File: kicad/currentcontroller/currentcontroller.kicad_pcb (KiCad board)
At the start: 2 copper layers, 86.4 x 53.3 mm, 39 parts, among them J1 Conn_01x04, J3 Conn_01x02, J4 Conn_01x04, Q1 IRF540N, U1 LM358, U2 MCP4822, U3 PC817, U4 PC817, U5 ATmega328P-P, U6 LM317_TO-220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

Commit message: Missing 5V trace
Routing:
- net +5V: track 164.1 -> 190.7 mm, vias 1 -> 2
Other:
- board text added: "Current controller Isolated (5 kV max) 2022-Dez www.tspi.at"
- board text removed: "Current controller Isolated (5 kV max) 76b595f / 2022-Nov www.tspi.at"
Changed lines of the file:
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@@
   (gr_rect (start 157.48 76.2) (end 243.84 129.54) (layer "Edge.Cuts") (width 0.1) (fill none))
   (gr_rect (start 219.71 106.68) (end 222.885 123.19) (layer "Edge.Cuts") (width 0.1) (fill none))
-  (gr_text "Current controller\nIsolated (5 kV max)\n76b595f / 2022-Nov\nwww.tspi.at" (at 219.71 99.695) (layer "F.SilkS")
+  (gr_text "Current controller\nIsolated (5 kV max)\n2022-Dez\nwww.tspi.at" (at 219.71 99.695) (layer "F.SilkS")
     (effects (font (size 1 1) (thickness 0.15)) (justify left))
   )
@@
   )
   (segment (start 184.15 102.91) (end 185.42 104.18) (width 0.25) (layer "F.Cu") (net 1))
+  (segment (start 181.61 93.98) (end 184.15 96.52) (width 0.25) (layer "F.Cu") (net 1))
   (segment (start 218.948 111.257) (end 218.948 93.218) (width 0.6) (layer "F.Cu") (net 1))
   (segment (start 187.96 80.01) (end 189.738 78.232) (width 0.25) (layer "F.Cu") (net 1))
@@
   (segment (start 185.42 104.18) (end 185.42 114.3) (width 0.25) (layer "F.Cu") (net 1))
   (segment (start 165.7325 112.99) (end 166.615 113.8725) (width 0.6) (layer "F.Cu") (net 1))
+  (segment (start 184.15 96.52) (end 184.15 102.91) (width 0.25) (layer "F.Cu") (net 1))
   (segment (start 185.674 125.984) (end 186.182 126.492) (width 0.6) (layer "F.Cu") (net 1))
   (segment (start 213.36 86.36) (end 215.9 86.36) (width 0.25) (layer "F.Cu") (net 1))
@@
   (segment (start 189.738 78.232) (end 198.882 78.232) (width 0.25) (layer "F.Cu") (net 1))
   (segment (start 185.42 125.984) (end 185.674 125.984) (width 0.6) (layer "F.Cu") (net 1))
+  (via (at 181.61 93.98) (size 0.8) (drill 0.4) (layers "F.Cu" "B.Cu") (net 1))
   (via (at 191.008 104.14) (size 0.8) (drill 0.4) (layers "F.Cu" "B.Cu") (net 1))
   (segment (start 185.38 104.14) (end 191.008 104.14) (width 0.25) (layer "B.Cu") (net 1))
   (segment (start 184.15 102.91) (end 185.38 104.14) (width 0.25) (layer "B.Cu") (net 1))
+  (segment (start 187.96 80.01) (end 184.333601 83.636399) (width 0.25) (layer "B.Cu") (net 1))
+  (segment (start 181.61 90.17) (end 181.61 93.98) (width 0.25) (layer "B.Cu") (net 1))
+  (segment (start 184.333601 83.636399) (end 184.333601 87.446399) (width 0.25) (layer "B.Cu") (net 1))
   (segment (start 185.42 125.73) (end 186.182 126.492) (width 0.25) (layer "B.Cu") (net 1))
   (segment (start 185.42 114.3) (end 185.42 125.73) (width 0.25) (layer "B.Cu") (net 1))
+  (segment (start 184.333601 87.446399) (end 181.61 90.17) (width 0.25) (layer "B.Cu") (net 1))
   (segment (start 162.56 109.22) (end 162.56 107.99) (width 0.25) (layer "F.Cu") (net 2))
   (segment (start 167.315 109.6475) (end 167.315 110.815) (width 0.25) (layer "F.Cu") (net 2))
@@
     (connect_pads (clearance 0.508))
     (min_thickness 0.254) (filled_areas_thickness no)
-    (fill yes (thermal_gap 0.508) (thermal_bridge_width 0.508) (smoothing fillet))
+    (fill (thermal_gap 0.508) (thermal_bridge_width 0.508) (smoothing fillet))
     (polygon
       (pts

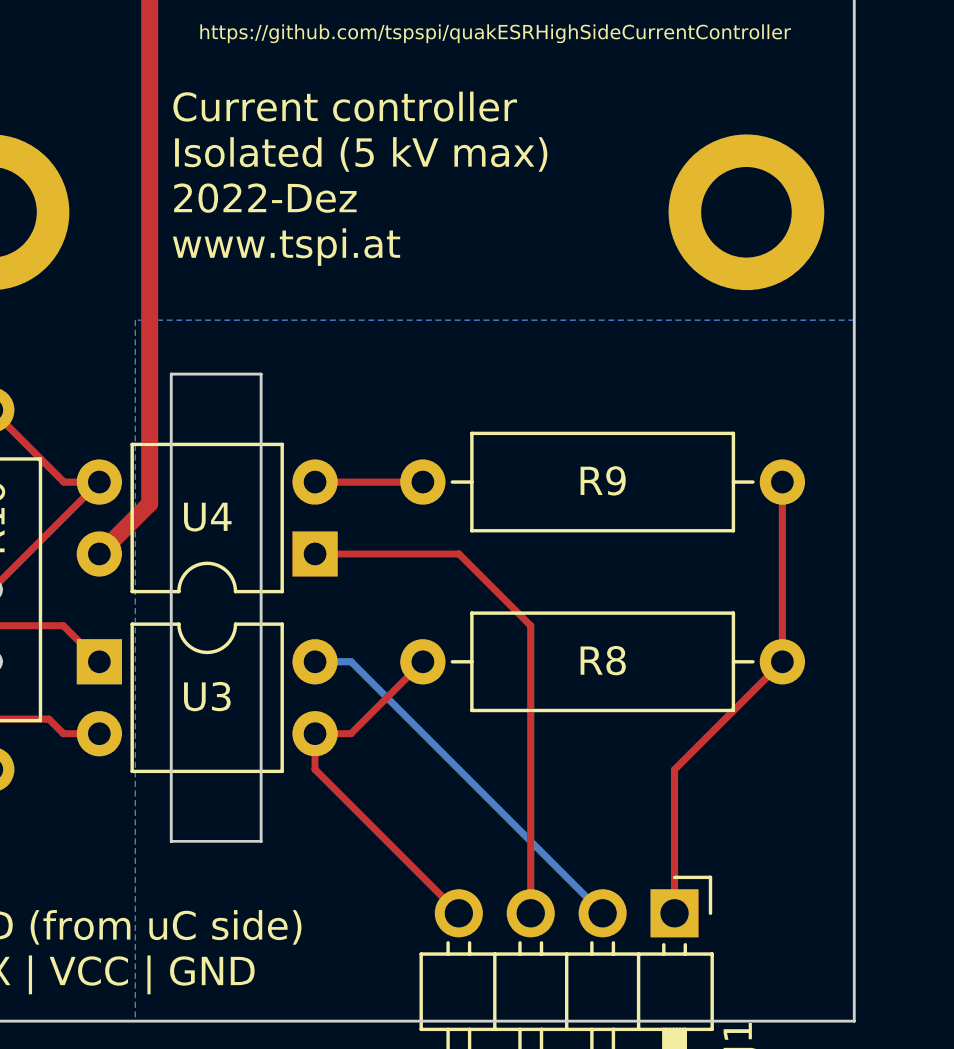
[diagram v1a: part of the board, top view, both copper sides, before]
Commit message: Added commit ID
* Added commit ID
* Added a second slot for isolated island
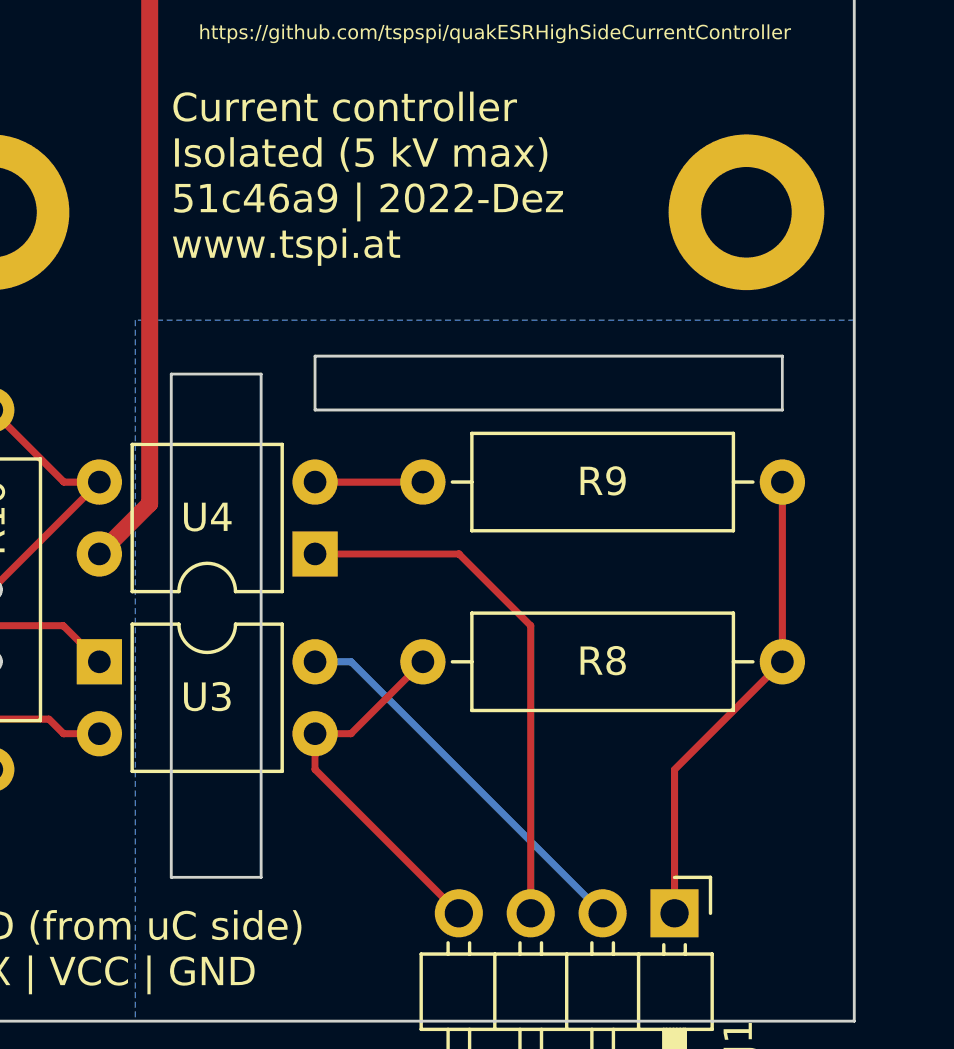
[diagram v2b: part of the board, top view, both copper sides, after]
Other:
- outline, holes or cut-outs redrawn
- board text added: "Current controller Isolated (5 kV max) 51c46a9 | 2022-Dez www.tspi.at"
- board text removed: "Current controller Isolated (5 kV max) 2022-Dez www.tspi.at"
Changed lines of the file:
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@@
   )
   (gr_rect (start 157.48 76.2) (end 243.84 129.54) (layer "Edge.Cuts") (width 0.1) (fill none))
-  (gr_rect (start 219.71 106.68) (end 222.885 123.19) (layer "Edge.Cuts") (width 0.1) (fill none))
-  (gr_text "Current controller\nIsolated (5 kV max)\n2022-Dez\nwww.tspi.at" (at 219.71 99.695) (layer "F.SilkS")
+  (gr_rect (start 224.79 107.95) (end 241.3 106.045) (layer "Edge.Cuts") (width 0.1) (fill none))
+  (gr_rect (start 219.71 106.68) (end 222.885 124.46) (layer "Edge.Cuts") (width 0.1) (fill none))
+  (gr_text "Current controller\nIsolated (5 kV max)\n51c46a9 | 2022-Dez\nwww.tspi.at" (at 219.71 99.695) (layer "F.SilkS")
     (effects (font (size 1 1) (thickness 0.15)) (justify left))
   )
@@
     (connect_pads (clearance 0.508))
     (min_thickness 0.254) (filled_areas_thickness no)
-    (fill (thermal_gap 0.508) (thermal_bridge_width 0.508) (smoothing fillet))
+    (fill yes (thermal_gap 0.508) (thermal_bridge_width 0.508) (smoothing fillet))
     (polygon
       (pts
